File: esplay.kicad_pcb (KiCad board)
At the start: 2 copper layers, 155 x 60 mm, 118 parts, among them J1 USB_C_Receptacle_USB2.0_16P, J2 Audio Jack, J3 ILI9341 3.2", J4 Battery, J5 Speaker, Q1 MMBT2222A, Q2 MMBT2222A, Q3 MMBT2222A, Q4 IRLML6402, SW1 Reset, SW10 L_BTN, SW11 MENU, SW12 R_BTN, SW13 SW_SPDT, SW14 C, SW15 D, SW2 UP, SW3 DOWN, SW4 LEFT, SW5 RIGHT, SW6 START, SW7 SELECT, SW8 A, SW9 B, U1 ESP32-WROVER-I, U10 LMC555xM, U2 PCF8574T, U3 CH340G, U4 LTC4054ES5-4.2, U5 MIC5219-3.3YM5, U6 UDA1334ATS, U7 PAM8403D, U8 MicroSD, U9 LMC555xM, Y1 12MHz

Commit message: Final revA
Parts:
- added BAT+1: +, TestPoint:TestPoint_Pad_D3.0mm, B.Cu at (33.0, 62.5)
- added BAT-1: -, TestPoint:TestPoint_Pad_D3.0mm, B.Cu at (33.0, 75.5)
- added G***: LOGO, footprints:andy_karpov_logo4_silk, B.Cu at (90.8, 63.8)
- added REF**: OSHW-Logo2_7.3x6mm_SilkScreen, Symbol:OSHW-Logo2_7.3x6mm_SilkScreen, B.Cu at (125.2, 90.2)
- added REF**: WEEE-Logo_5.6x8mm_SilkScreen, Symbol:WEEE-Logo_5.6x8mm_SilkScreen, B.Cu at (170.2, 88.8)
- added REF**: KiCad-Logo2_5mm_SilkScreen, Symbol:KiCad-Logo2_5mm_SilkScreen, B.Cu at (40.0, 53.8)
- J4: footprint Connector_JST:JST_PH_S2B-PH-SM4-TB_1x02-1MP_P2.00mm_Horizontal -> Connector_JST:JST_PH_S2B-PH-K_1x02_P2.00mm_Horizontal
- moved J4 56.8 mm to (32.8, 68.0), turned to -90 degrees
- moved C7 49.9 mm to (38.5, 81.0)
- moved R26 1.75 mm to (51.2, 87.0), turned to 0 degrees
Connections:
- J4 pad 1: GND -> V_BATT
- J4 pad 2: V_BATT -> GND
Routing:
- net VCC3_3: track 369.6 -> 411.8 mm, vias 12 -> 26
- net V_USB: track 38.1 -> 68.3 mm, vias 0 -> 4
- net V_BATT: track 68.2 -> 88.3 mm, vias 3 -> 6
- net GND: track 21.0 -> 30.2 mm, vias 53 -> 133
- net D-: track 12.3 -> 20.7 mm, vias 0 -> 2
- net D+: track 12.2 -> 16.8 mm, vias 0 -> 2
- net VIN: track 134.8 -> 136.1 mm, vias 3 -> 6
- net TX: track 49.8 -> 48.7 mm
- net Net-(J1-CC1): track 5.24 -> 5.93 mm
- net L_BTN: track 81.4 -> 82.0 mm
- net SELECT: track 56.1 -> 55.5 mm
- net START: track 44.0 -> 43.4 mm
- net DOWN: track 38.0 -> 37.5 mm
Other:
- board text added: "(с) 2025"
- board text added: "Karabas ESPlay"
- board text added: "OFF"
- board text added: "ON"
- board text added: "POWER"
- board text added: "rev.${REVISION}"

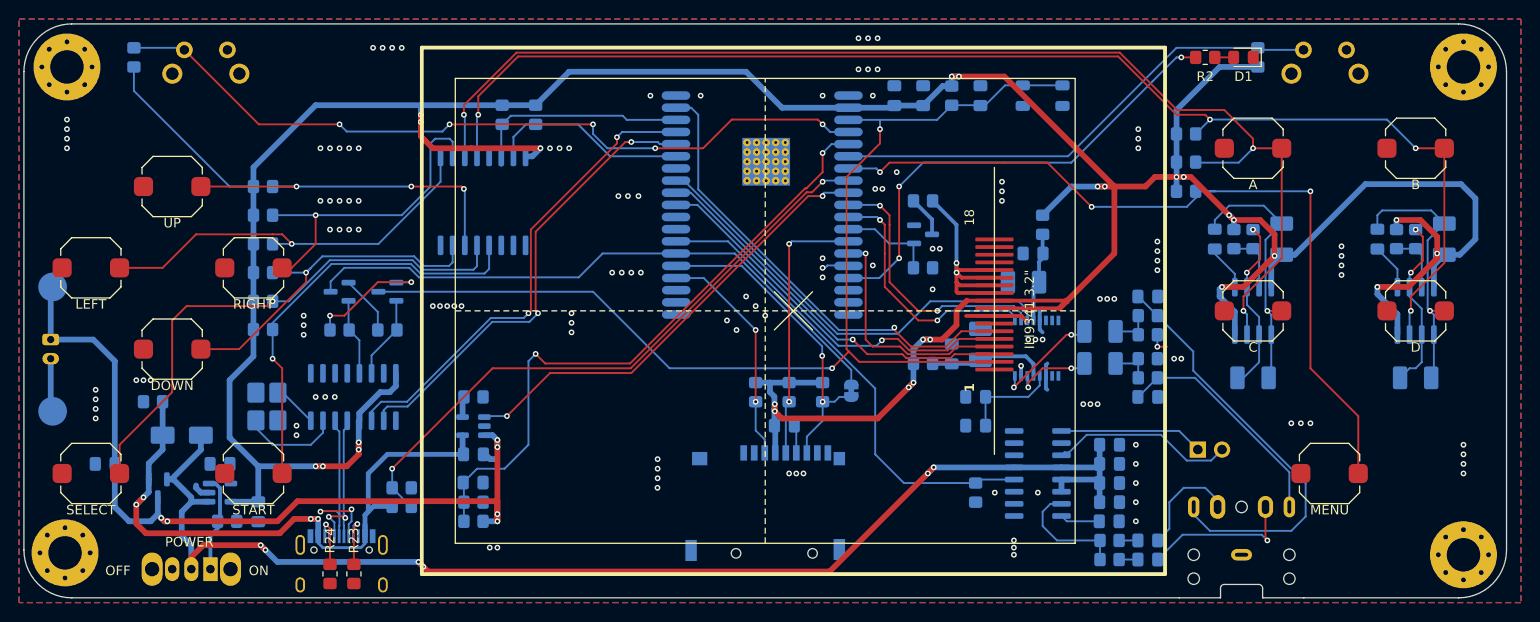
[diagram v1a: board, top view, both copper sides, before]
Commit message: added keepout area to the wifi antenna
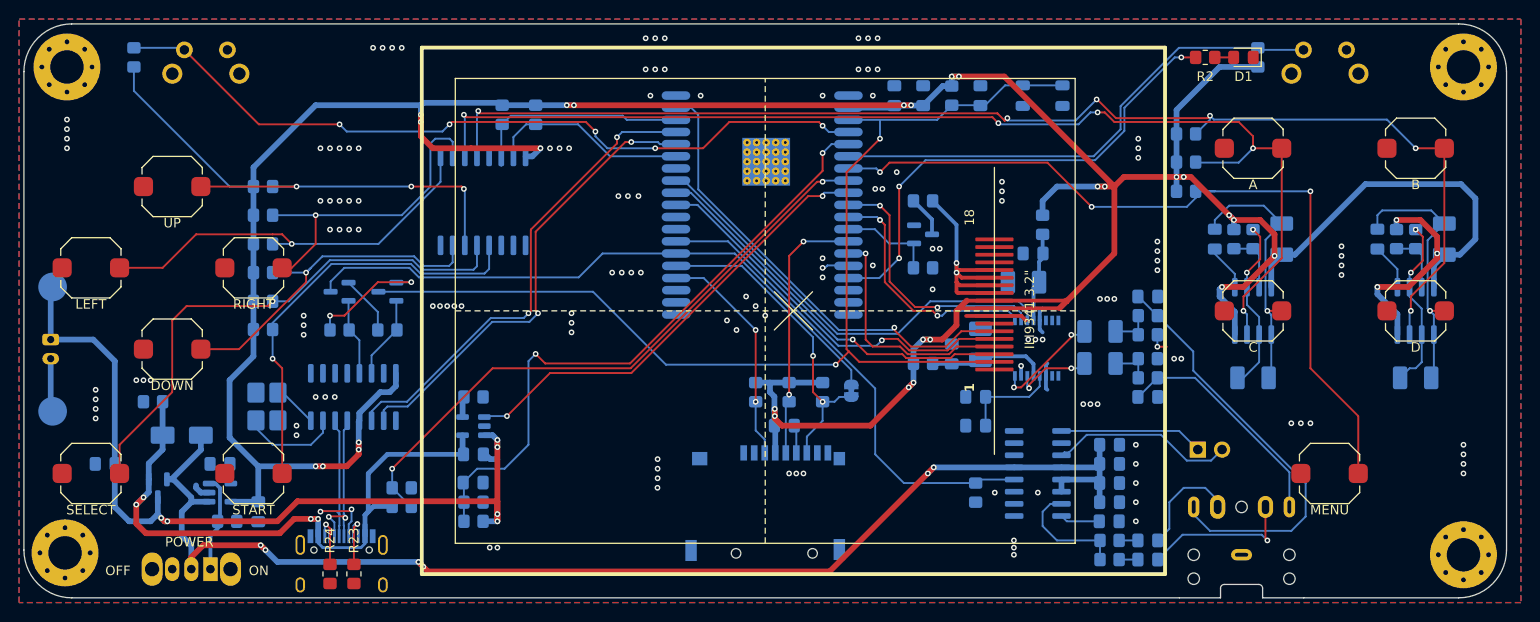
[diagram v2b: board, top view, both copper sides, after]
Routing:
- net VCC3_3: track 411.8 -> 421.4 mm, vias 26 -> 30
- net A: track 125.8 -> 121.0 mm, vias 3 -> 5
- net B: track 136.1 -> 133.5 mm, vias 4 -> 6
- net R_BTN: track 52.4 -> 53.8 mm
- net Net-(U1-IO13): track 50.2 -> 51.7 mm
- net RESET: track 119.2 -> 118.2 mm
- net I2S_BCK: track 26.7 -> 26.0 mm
- net GND: vias 133 -> 139

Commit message: Added revA2
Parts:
- removed the REF** at (170.2, 88.8)
- SW11, SW14, SW15, SW2, SW3, SW4, SW5, SW6, SW7, SW8, SW9: footprint Button_Switch_SMD:SW_Push_1TS009xxxx-xxxx-xxxx_6x6x5mm -> footprints:SW_Push_1TS009_combined1
- moved C5 2.30 mm to (49.0, 79.2)
- moved U5 2.30 mm to (49.0, 82.2)
- moved R26 2.00 mm to (51.2, 85.0)
- moved D2 1.50 mm to (46.5, 76.5)
- moved R25 1.50 mm to (43.5, 73.0)
- moved C6 1.41 mm to (55.5, 85.0), turned to 0 degrees
- moved Q4 1.30 mm to (44.0, 82.2)
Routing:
- net LEFT: track 42.8 -> 55.8 mm
- net GND: track 30.2 -> 42.1 mm, vias 139 -> 143
- net DOWN: track 37.5 -> 46.1 mm
- net B: track 133.5 -> 142.0 mm
- net Net-(U9-GND): track 28.1 -> 35.7 mm
- net Net-(U10-GND): track 28.0 -> 35.6 mm
- net UP: track 36.0 -> 43.7 mm
- net RIGHT: track 34.0 -> 41.3 mm
- net Net-(SW13-A): track 10.2 -> 15.8 mm, vias 0 -> 4
- net SELECT: track 55.5 -> 60.0 mm
- net START: track 43.4 -> 47.3 mm
- net MENU: track 83.9 -> 87.8 mm
- net A: track 121.0 -> 124.5 mm, vias 5 -> 6
- net VIN: track 136.1 -> 139.5 mm, vias 6 -> 10
- net VCC3_3: track 421.4 -> 423.0 mm
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
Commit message: revA3
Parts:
- U6: footprint Package_SO:SSOP-16_4.4x5.2mm_P0.65mm -> footprints:SSOP-16_4.4x5.2mm_P0.65mm-extended
- moved SW14 24.0 mm to (175.5, 48.0)
- moved SW15 24.0 mm to (158.5, 48.0)
- moved SW8 24.0 mm to (175.5, 65.0)
- moved SW9 24.0 mm to (158.5, 65.0)
- moved C27 17.1 mm to (175.6, 71.9)
- moved C29 17.1 mm to (178.6, 57.4)
- moved R43 17.1 mm to (175.6, 57.4)
- moved R44 17.1 mm to (173.6, 57.4)
- moved U9 17.1 mm to (175.6, 64.9)
- moved C28 17.0 mm to (171.5, 57.5)
- moved C30 17.0 mm to (161.5, 57.5)
- moved C31 17.0 mm to (158.5, 72.0)
- moved C32 17.0 mm to (154.5, 57.5)
- moved R41 17.0 mm to (156.5, 57.5)
- moved R42 17.0 mm to (158.5, 57.5)
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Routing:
- net B: track 142.0 -> 121.4 mm, vias 6 -> 8
- net A: track 124.5 -> 130.4 mm, vias 6 -> 7
- net GND: track 42.1 -> 46.0 mm
- net Net-(U10-GND): track 35.6 -> 39.2 mm
- net Net-(U9-GND): track 35.7 -> 39.2 mm
- net MENU: track 87.8 -> 86.6 mm
- net VCC3_3: track 423.0 -> 422.0 mm, vias 30 -> 31
- net Net-(U9-THR): track 18.2 -> 17.6 mm
- net Net-(U6-VOUTL): track 8.43 -> 9.01 mm
